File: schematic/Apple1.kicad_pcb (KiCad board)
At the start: 4 copper layers, 8.2 x 91 mm, 68 parts, among them J1 PWR, J2 EDGE, J3 SLOT, J4 12V, J5 -12V, J6 Micro_SD_Card_Det, J7 RCJ-041, J8 USB_A, J9 HDMI_A, Q1 DMG1012T, Q2 DMG1012T, SW1 PWR, SW2 RST, SW3 CLEAR, U1 WD65C02, U10 AP7315DQ-2.5, U11 TXB0104D, U12 TXB0104D, U13 TXB0104D, U14 TXB0104D, U15 TXB0104D, U16 ESD5384, U17 AP2331W, U2 6821 (W65C21N), U3 AS6C62256, U4 AT28C64B-15PU, U5 74LS138, U6 RaspberryPi-CM3+L, U7 L7805, U8 PAM2306AYPKE, U9 74HC00

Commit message: finished product v1
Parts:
- removed C17, C18, C19: 47uF, Capacitor_SMD:C_1206_3216Metric
- removed C20: 4.7uF, Capacitor_SMD:C_0603_1608Metric_Pad1.08x0.95mm_HandSolder
- removed C21, C22, C3: 0.1uF, Capacitor_SMD:C_0603_1608Metric_Pad1.08x0.95mm_HandSolder
- removed C4, C5, C6, C7: 10uF, Capacitor_SMD:C_0603_1608Metric_Pad1.08x0.95mm_HandSolder
- removed C8, C9: 0.47uF, Capacitor_SMD:C_0603_1608Metric_Pad1.08x0.95mm_HandSolder
- removed J6: Micro_SD_Card_Det, Connector_Card:microSD_HC_Molex_104031-0811
- removed J7: RCJ-041, CUI_RCJ-041
- removed J8: USB_A, UJ2-AH-4-TH:CUI_UJ2-AH-4-TH
- removed J9: HDMI_A, 10029449-111RLF:10029449111RLF
- removed L1, L2: 4.7uH, Inductor_SMD:L_Bourns-SRN4018
- removed Q1, Q2: DMG1012T, Package_TO_SOT_SMD:SOT-523
- removed R10, R11, R4, R7, R8, R9: 100k, Resistor_SMD:R_0603_1608Metric
- removed U10: AP7315DQ-2.5, Package_TO_SOT_SMD:SOT-23-5
- removed U16: ESD5384, SW-On-Semi:WLCSP9-1.14x1.14mm
- removed U17: AP2331W, Package_TO_SOT_SMD:SOT-23
- removed U8: PAM2306AYPKE, Package_DFN_QFN:WDFN-12-1EP_3x3mm_P0.45mm_EP1.7x2.5mm
- U6: value RaspberryPi-CM3+L -> Raspberry_Pi_Zero; footprint 1717254-4:17172544 -> Connector:Raspberry_Pi_Zero
- moved U6 29.9 mm to (173.2, 45.1), turned to 90 degrees
- moved D2 12.8 mm to (127.0, 50.7)
- moved R6 12.8 mm to (141.8, 53.7)
- moved SW1 12.8 mm to (142.1, 41.6)
- moved U7 12.8 mm to (152.8, 41.7)
- moved C1 12.8 mm to (153.3, 46.2)
- moved C2 12.8 mm to (157.4, 46.2)
- moved J1 12.8 mm to (123.1, 43.5)
- moved D1 12.8 mm to (147.0, 47.7)
- moved U14 5.33 mm to (219.4, 67.7)
- moved U11 5.33 mm to (229.9, 67.8)
- moved U12 5.33 mm to (209.0, 67.7)
- moved U13 5.33 mm to (187.8, 67.7)
- moved U15 5.33 mm to (198.4, 67.7)
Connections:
- U6 pad 1: GND -> +3V3
- U6 pad 10: /RaspberryPi/SDX_CLK -> /RaspberryPi/RP_OEA
- U6 pad 12: /RaspberryPi/SDX_CMD -> /RaspberryPi/RP_PA3
- U6 pad 13: GND -> /RaspberryPi/RP_PA4
- U6 pad 15: (no net) -> /RaspberryPi/RP_PA5
- U6 pad 16: /RaspberryPi/SDX_D0 -> /RaspberryPi/RP_PA6
- U6 pad 17: (no net) -> +3V3
- U6 pad 18: /RaspberryPi/SDX_D1 -> (no net)
- U6 pad 19: GND -> /RaspberryPi/RP_PB0
- U6 pad 2: (no net) -> +5V
- U6 pad 21: (no net) -> /RaspberryPi/RP_PB1
- U6 pad 22: /RaspberryPi/SDX_D2 -> /RaspberryPi/RP_PB2
- U6 pad 23: (no net) -> /RaspberryPi/RP_PB3
- U6 pad 24: /RaspberryPi/SDX_D3 -> /RaspberryPi/RP_OEB
- U6 pad 26: GND -> /RaspberryPi/RP_PB4
- U6 pad 28: /RaspberryPi/RP_STB -> (no net)
- U6 pad 29: (no net) -> /RaspberryPi/RP_PB5
- U6 pad 3: (no net) -> /RaspberryPi/RP_STB
- U6 pad 30: /RaspberryPi/RP_PA0 -> GND
- U6 pad 31: GND -> /RaspberryPi/RP_PB6
- U6 pad 32: GND -> /RaspberryPi/RP_DA
- U6 pad 33: (no net) -> /RaspberryPi/RP_RDA
- U6 pad 34: /RaspberryPi/RP_PA1 -> GND
- U6 pad 35: (no net) -> /RaspberryPi/RP_PHI2
- U6 pad 36: /RaspberryPi/RP_PA2 -> /RaspberryPi/RP_CB2
- U6 pad 37: GND -> /RaspberryPi/RP_OEC
- U6 pad 38: GND -> /RaspberryPi/RP_RST
- U6 pad 39: +3V3 -> GND
- U6 pad 4: +3V3 -> +5V
- U6 pad 40: +3V3 -> /RaspberryPi/CLEAR
- U6 pad 5: (no net) -> /RaspberryPi/RP_PA0
- U6 pad 6: +3V3 -> GND
- U6 pad 7: GND -> /RaspberryPi/RP_PA2
- U6 pad 8: GND -> /RaspberryPi/RP_PA1
- U6 pad 9: (no net) -> GND
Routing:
- net /RESET: track 34.2 -> 349.5 mm, vias 0 -> 3
- net /PHI2O: track 80.5 -> 234.6 mm, vias 0 -> 2
- net GND: track 214.4 -> 358.3 mm, vias 1 -> 8
- net /NMI: track 12.7 -> 150.5 mm
- net /IQR: track 12.7 -> 150.3 mm
- net /RDY: track 12.7 -> 148.1 mm
- net /SYNC: track 15.6 -> 150.1 mm
- net /PHI1O: track 15.6 -> 145.3 mm
- net /A14: track 197.5 -> 325.7 mm, vias 0 -> 1
- net /A13: track 186.7 -> 313.0 mm, vias 0 -> 1
- net /A12: track 220.2 -> 339.6 mm, vias 0 -> 1
- net +12V: track 26.5 -> 145.8 mm
- net /$C000: track 9.24 -> 120.6 mm, vias 0 -> 1
- net /A10: track 187.7 -> 290.9 mm, vias 1 -> 2
- net /A15: track 186.0 -> 285.4 mm, vias 0 -> 2
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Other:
- board size 8.2 x 91 mm -> 149 x 134.7 mm

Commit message: finished apple 1
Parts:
- added G1: LOGO, Apple1Title:title, F.Cu at (131.5, 64.2)
- added G2: LOGO, Apple1Title:n12v, F.Cu at (249.4, 36.2)
- added G3: LOGO, Apple1Title:12v, F.Cu at (245.3, 36.5)
- C1, C2: footprint Capacitor_SMD:C_0603_1608Metric_Pad1.08x0.95mm_HandSolder -> Capacitor_THT:C_Rect_L7.0mm_W2.5mm_P5.00mm
- moved C1 1.39 mm to (152.4, 45.1), turned to 270 degrees
- moved C2 1.36 mm to (158.2, 45.1), turned to 270 degrees
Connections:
- J3 pad MH1: GND -> (no net)
- J3 pad MH2: GND -> (no net)
- U6 pad MT: GND -> (no net)
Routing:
- net +5V: track 513.8 -> 527.2 mm
- net GND: track 358.3 -> 360.2 mm, vias 8 -> 11
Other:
- net class All: via_drill 0.7 -> 0.65
- net class Default: via_drill 0.7 -> 0.65
- net class HDMI: via_drill 0.7 -> 0.65
- net class PWR: via_drill 0.7 -> 0.65
- net class RPi: via_drill 0.7 -> 0.65
- net class USB_dPair: via_drill 0.7 -> 0.65

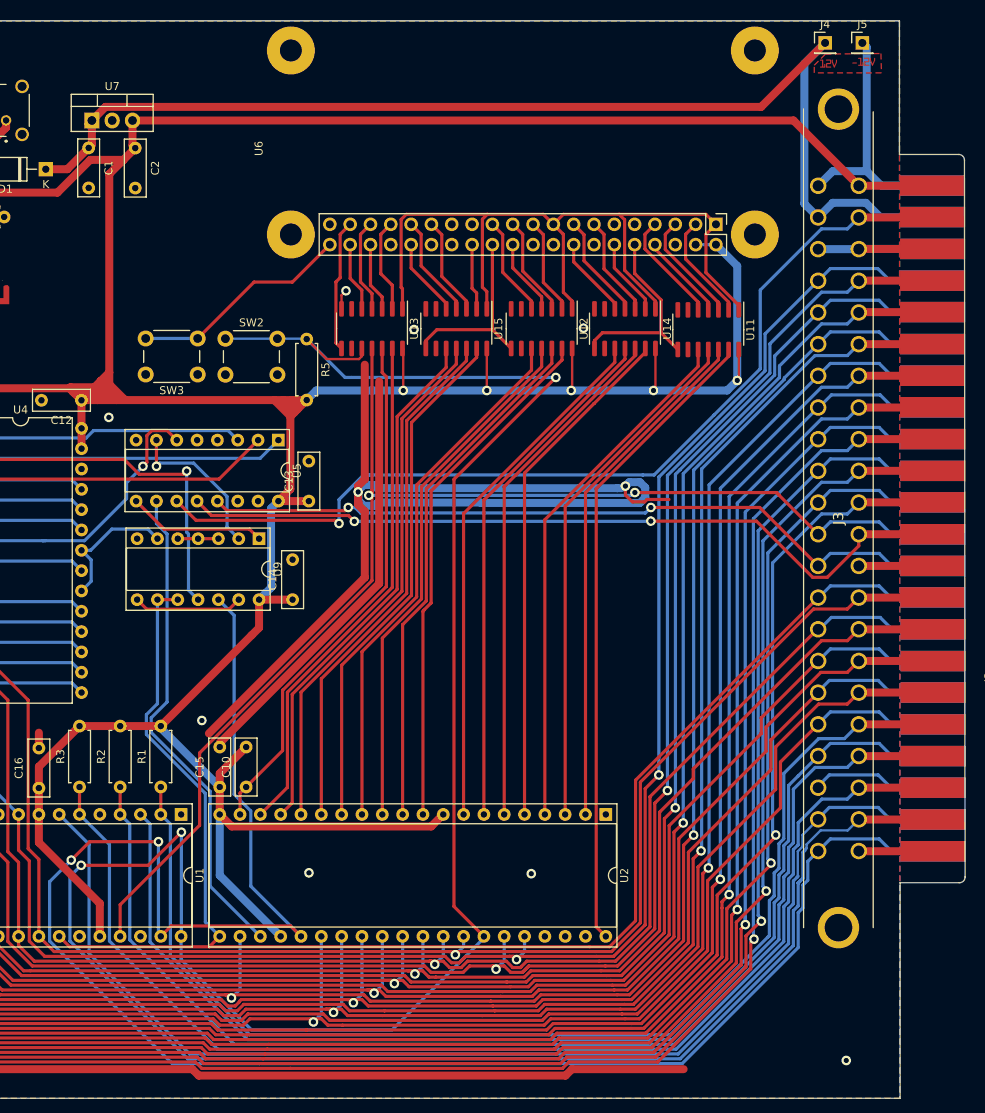
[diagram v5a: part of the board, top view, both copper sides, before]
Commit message: updated edgeconnector footprint
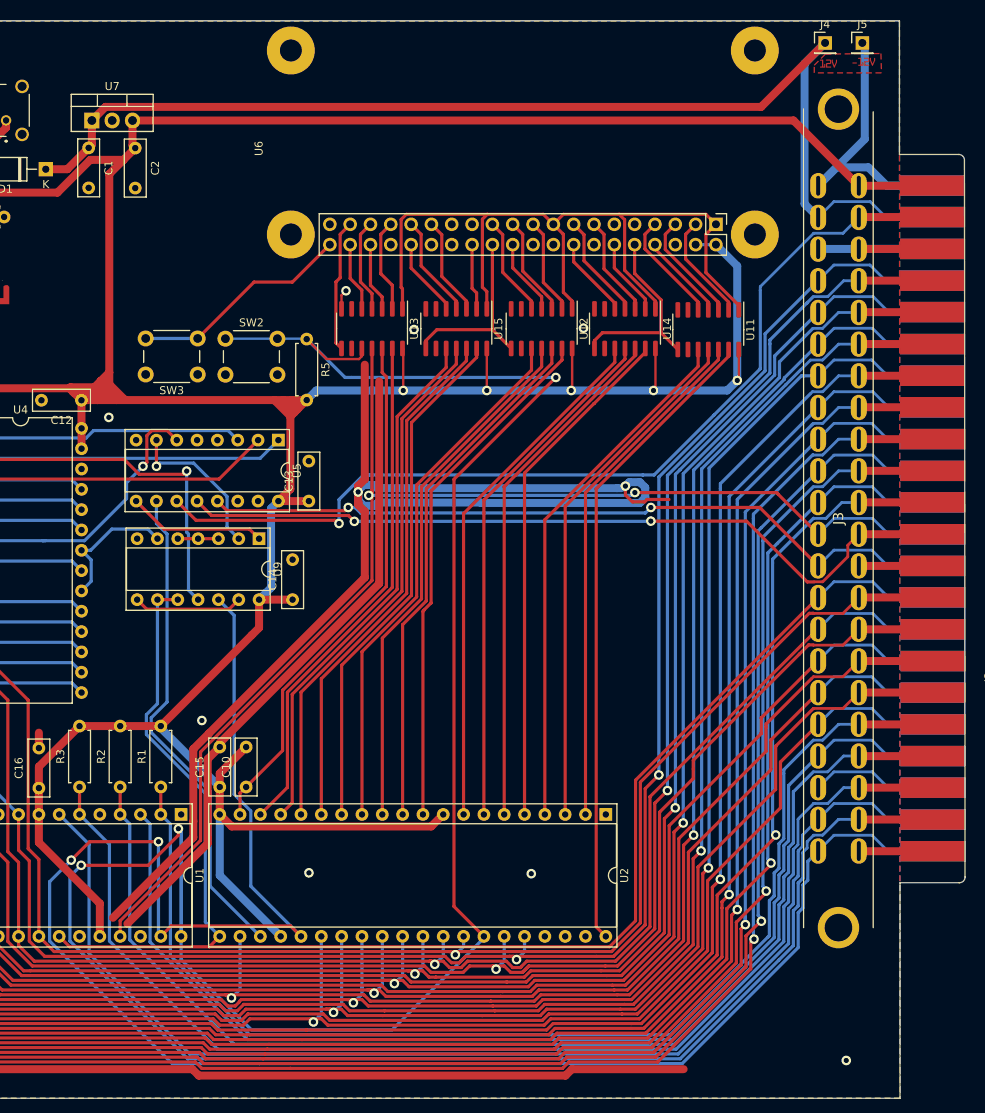
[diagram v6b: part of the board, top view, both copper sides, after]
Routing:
- net GND: track 360.2 -> 424.3 mm
- net /RESET: track 349.5 -> 362.6 mm
- net -12V: track 32.0 -> 36.6 mm
- net /A6: track 293.2 -> 294.8 mm
- net /D2: track 209.8 -> 210.4 mm
- net /A9: track 297.2 -> 297.7 mm
